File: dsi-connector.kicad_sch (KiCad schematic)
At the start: 13 parts, among them J1 Plug_Molex_SlimStack_2x20_556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

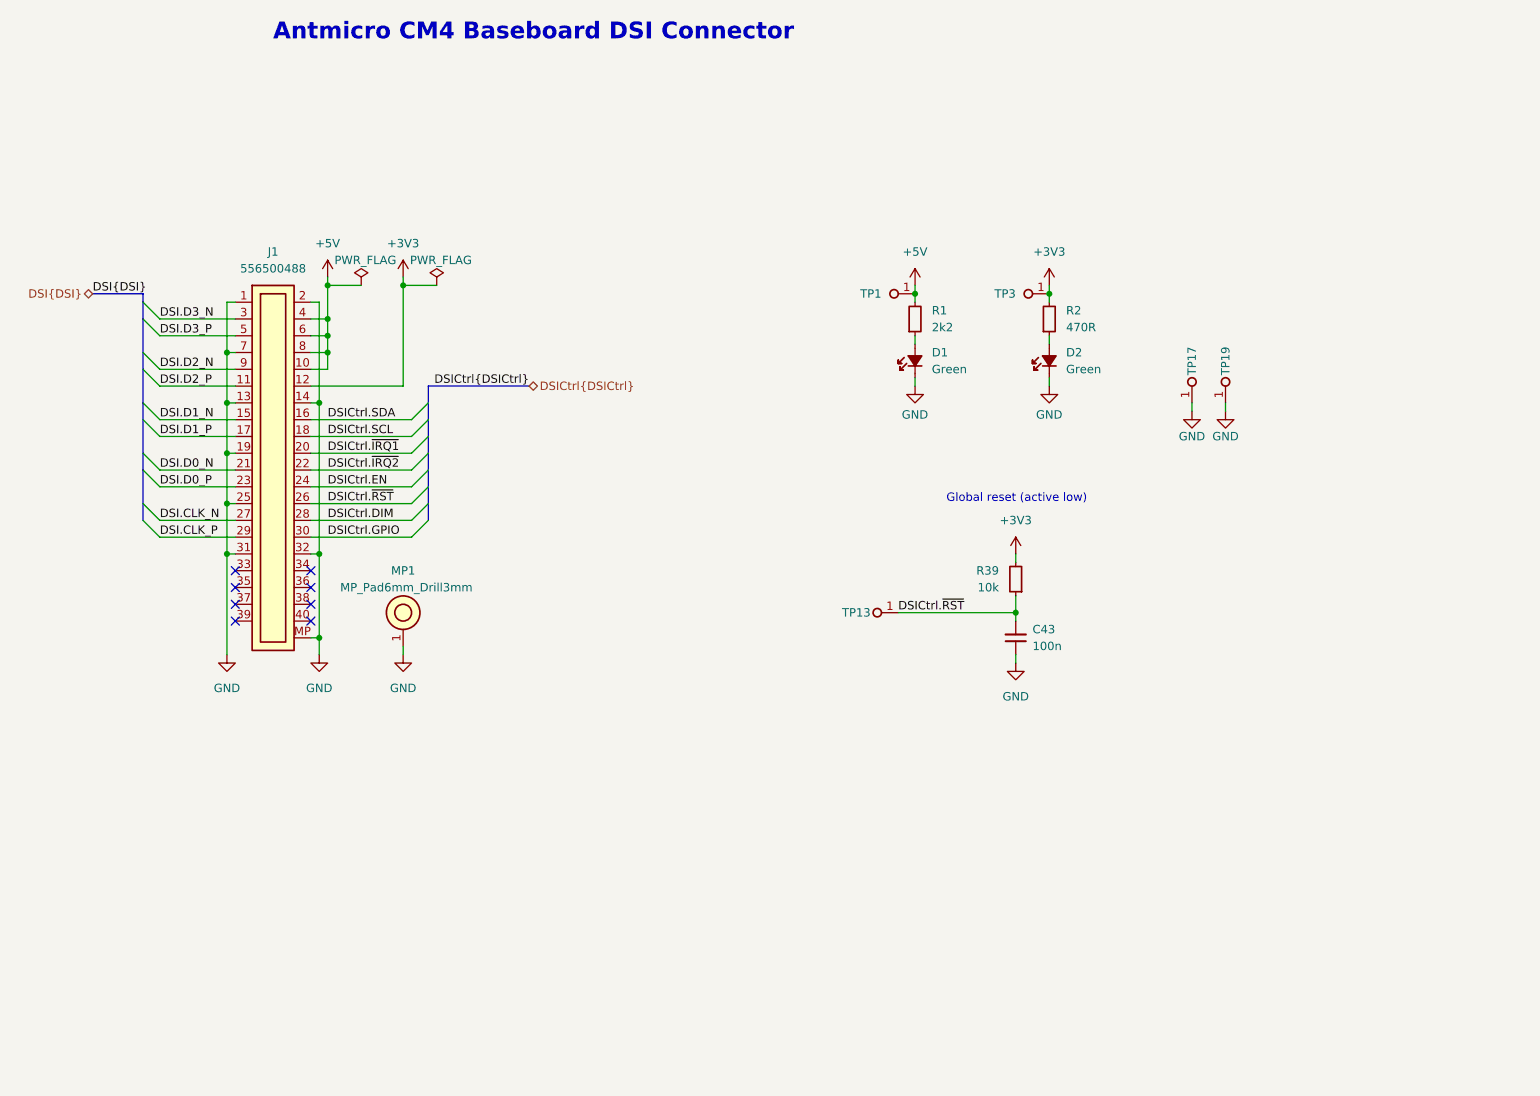
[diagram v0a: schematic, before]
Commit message: [#73840] Bump rev to 1.1.3, Standarize Sch
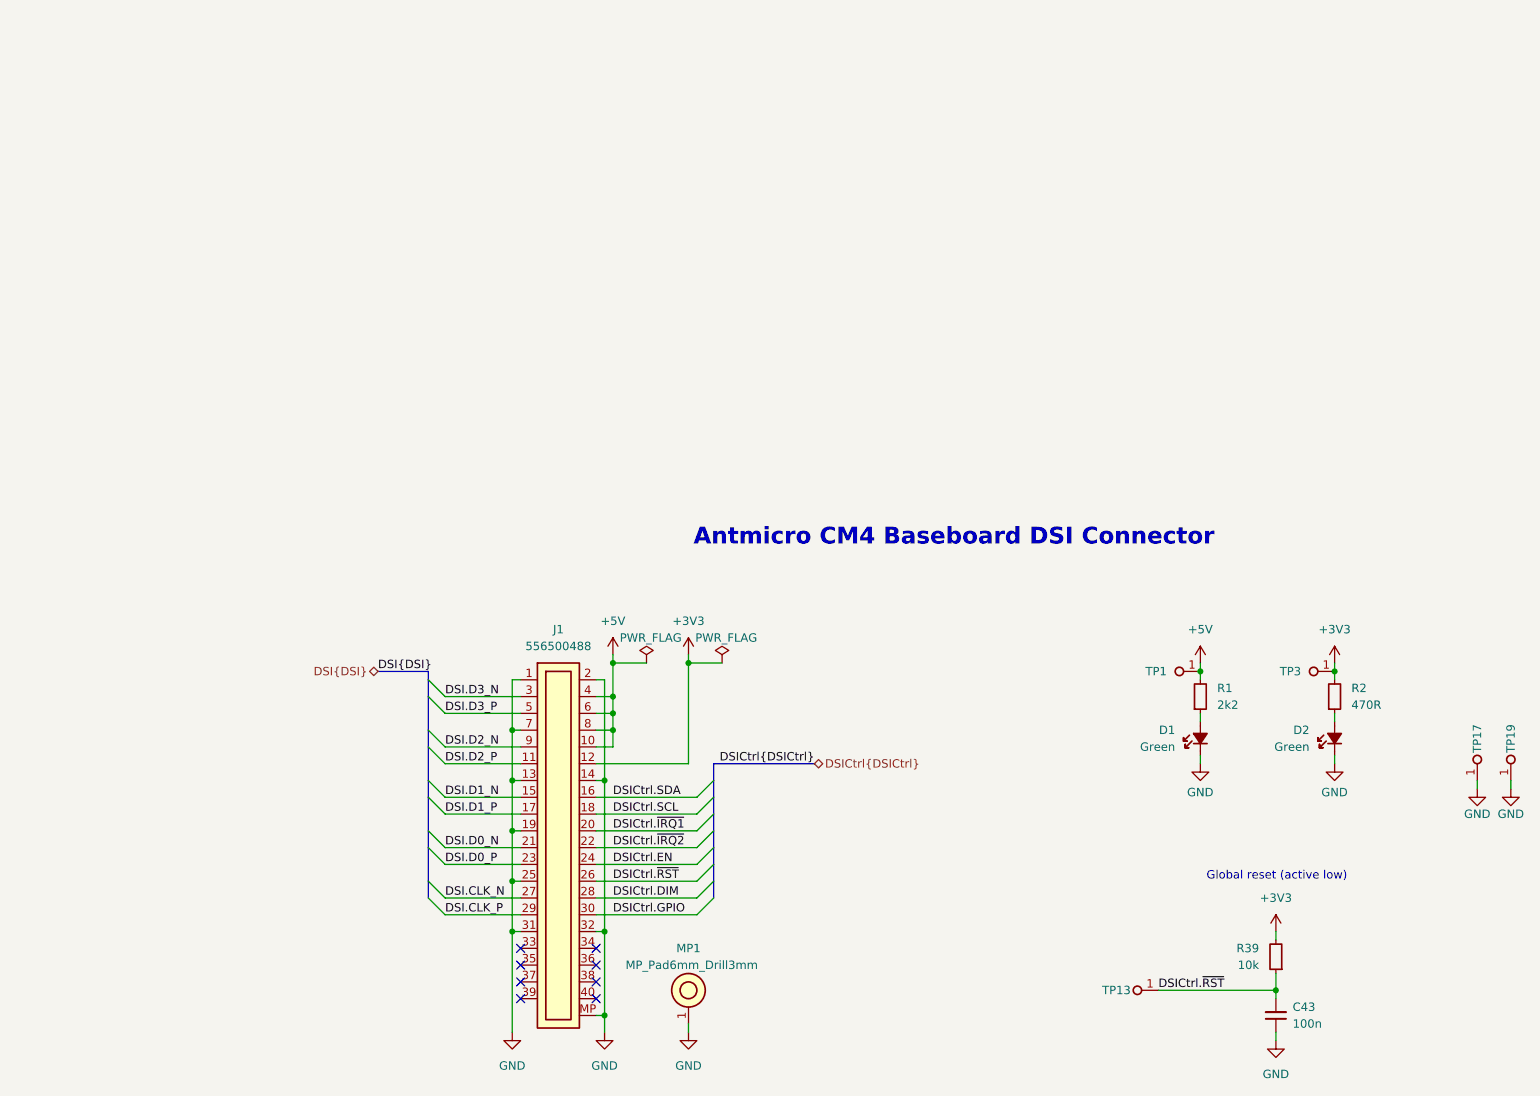
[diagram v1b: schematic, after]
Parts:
- C43, MP1, R1, R2, R39, TP1, TP3: Public False -> (none)
- D1, D2: footprint antmicro-footprints:LED_0603_1608Metric_G -> antmicro-footprints:LED_0603_1608Metric_G_Right_Angle; Public False -> (none)
- TP13, TP17, TP19: Public False -> (none); now left out of the parts list
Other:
- moved on the sheet: C43, D1, D2, J1, MP1, R1, R2, R39, TP1, TP13, TP17, TP19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

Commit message: [#73840] Change right angle LEDs to vertical (KP-1608ZGC)
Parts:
- removed D1, D2: LED_G_0603_598-8D80-107F, antmicro-footprints:LED_0603_1608Metric_G_Right_Angle, symbol antmicroLEDIndicationDiscrete:LED_G_0603_598-8D80-107F
- removed R1: R_2k2_0402, antmicro-footprints:R_0402_1005Metric, symbol antmicroResistors0402:R_2k2_0402
- removed R2: R_470R_0402, antmicro-footprints:R_0402_1005Metric, symbol antmicroResistors0402:R_470R_0402
- added D1, D2: LED_G_0603_KP-1608ZGC, antmicro-footprints:LED_0603_1608Metric_G, symbol antmicroLEDIndicationDiscrete:LED_G_0603_KP-1608ZGC
- added R1: R_470R_0402, antmicro-footprints:R_0402_1005Metric, symbol antmicroResistors0402:R_470R_0402
- added R3: R_330R_0402, antmicro-footprints:R_0402_1005Metric, symbol antmicroResistors0402:R_330R_0402
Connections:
- net +3V3: now also R3.2
- net +5V: now also R1.2
- net GND: now also D1.1 (C), D2.1 (C)
- new net: D2.2 (A), R3.1
- new net: D1.2 (A), R1.1

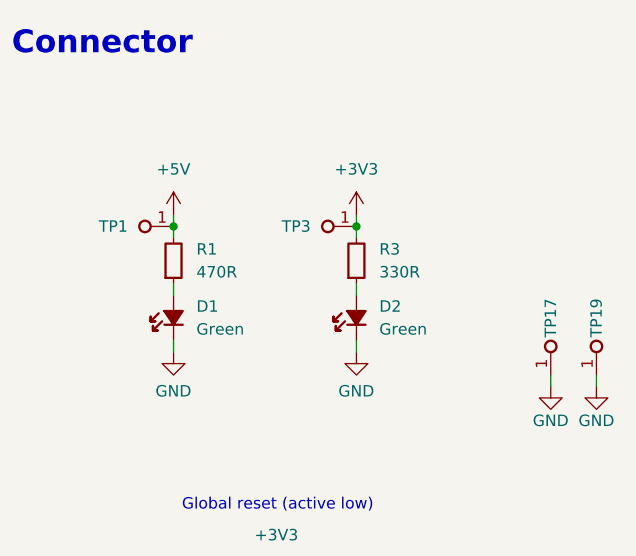
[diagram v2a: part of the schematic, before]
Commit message: [#73840] Update 3V3 LED resistors to 100R andd 10V5 LED resistors to 1k5
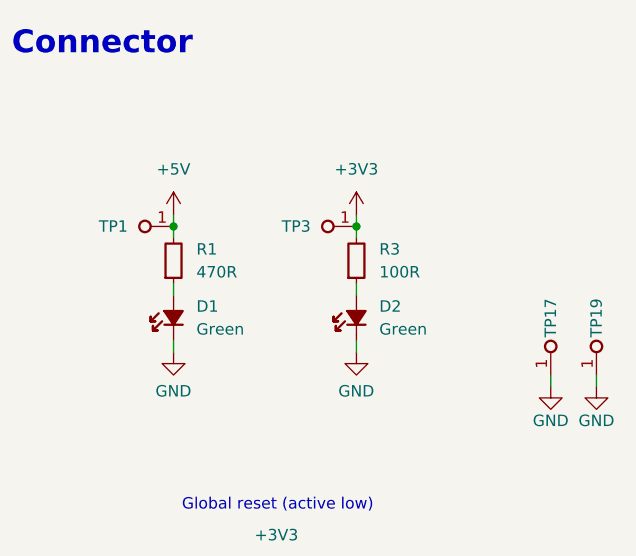
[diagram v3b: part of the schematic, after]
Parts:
- removed R3: R_330R_0402, antmicro-footprints:R_0402_1005Metric, symbol antmicroResistors0402:R_330R_0402
- added R3: R_100R_0402, antmicro-footprints:R_0402_1005Metric, symbol antmicroResistors0402:R_100R_0402
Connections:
- net +3V3: now also R3.2
- net at D2.2 (A): now also R3.1
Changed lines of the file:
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@@
+	)
+	(symbol
+		(lib_id "antmicroResistors0402:R_100R_0402")
+		(at 270.51 124.46 90)
+		(unit 1)
+		(exclude_from_sim no)
+		(in_bom yes)
+		(on_board yes)
+		(dnp no)
+		(fields_autoplaced yes)
+		(property "Reference" "R3"
+			(at 273.05 120.65 90)
+			(effects
+				(font
+					(size 1.27 1.27)
+					(thickness 0.15)
+				)
+				(justify right)
+			)
+		)
+		(property "Value" "R_100R_0402"
+			(at 283.21 104.14 0)
+			(effects
+				(font
+					(size 1.27 1.27)
+					(thickness 0.15)
+				)
+				(justify left bottom)
+				(hide yes)
+			)
+		)
+		(property "Footprint" "antmicro-footprints:R_0402_1005Metric"
+			(at 285.75 104.14 0)
+			(effects
+				(font
+					(size 1.27 1.27)
+					(thickness 0.15)
+				)
+				(justify left bottom)
+				(hide yes)
+			)
+		)
+		(property "Datasheet" "https://www.bourns.com/docs/product-datasheets/cr.pdf"
+			(at 288.29 104.14 0)
+			(effects
+				(font
+					(size 1.27 1.27)
+					(thickness 0.15)
+				)
+				(justify left bottom)
+				(hide yes)
+			)
+		)
+		(property "Description" "SMD Chip Resistor, 100 ohm, ± 1%, 62.5 mW, 0402 [1005 Metric], Thick Film, General Purpose"
+			(at 270.51 124.46 0)
+			(effects
+				(font
+					(size 1.27 1.27)
+				)
+				(hide yes)
+			)
+		)
+		(property "MPN" "CR0402-FX-1000GLF"
+			(at 290.83 104.14 0)
+			(effects
+				(font
+					(size 1.27 1.27)
+					(thickness 0.15)
+				)
+				(justify left bottom)
+				(hide yes)
+			)
+		)
+		(property "Manufacturer" "Bourns"
+			(at 293.37 104.14 0)
+			(effects
+				(font
+					(size 1.27 1.27)
+					(thickness 0.15)
+				)
+				(justify left bottom)
+				(hide yes)
+			)
+		)
+		(property "License" "Apache-2.0"
+			(at 295.91 104.14 0)
+			(effects
+				(font
+					(size 1.27 1.27)
+					(thickness 0.15)
+				)
+				(justify left bottom)
+				(hide yes)
+			)
+		)
+		(property "Author" "Antmicro"
+			(at 298.45 104.14 0)
+			(effects
+				(font
+					(size 1.27 1.27)
+					(thickness 0.15)
+				)
+				(justify left bottom)
+				(hide yes)
+			)
+		)
+		(property "Val" "100R"
+			(at 273.05 123.19 90)
+			(effects
+				(font
+					(size 1.27 1.27)
+					(thickness 0.15)
+				)
+				(justify right)
+			)
+		)
+		(property "Tolerance" "1%"
+			(at 280.67 104.14 0)
+			(effects
+				(font
+					(size 1.27 1.27)
+				)
+				(justify left bottom)
+				(hide yes)
+			)
+		)
+		(pin "2"
+		)
+		(pin "1"
+		)
+		(instances
+			(project ""
+				(path "/60b842dc-0853-4a25-99ac-5784ddf94d0d/22d16469-9258-4636-9009-0bef153eb515"
+					(reference "R3")
+					(unit 1)
+				)
+			)
+		)
 	)
 	(symbol
@@
 					(unit 1)
 				)
-			)
-		)
-	)
-	(symbol
-		(lib_id "antmicroResistors0402:R_330R_0402")
-		(at 270.51 124.46 90)
-		(unit 1)
-		(exclude_from_sim no)
-		(in_bom yes)
-		(on_board yes)
-		(dnp no)
-		(fields_autoplaced yes)
-		(property "Reference" "R3"
-			(at 273.05 120.65 90)
-			(effects
-				(font
-					(size 1.27 1.27)
-					(thickness 0.15)
-				)
-				(justify right)
-			)
-		)
-		(property "Value" "R_330R_0402"
-			(at 283.21 104.14 0)
-			(effects
-				(font
-					(size 1.27 1.27)
-					(thickness 0.15)
-				)
-				(justify left bottom)
-				(hide yes)
-			)
-		)
-		(property "Footprint" "antmicro-footprints:R_0402_1005Metric"
-			(at 285.75 104.14 0)
-			(effects
-				(font
-					(size 1.27 1.27)
-					(thickness 0.15)
-				)
-				(justify left bottom)
-				(hide yes)
-			)
-		)
-		(property "Datasheet" "https://www.bourns.com/docs/product-datasheets/cr.pdf"
-			(at 288.29 104.14 0)
-			(effects
-				(font
-					(size 1.27 1.27)
-					(thickness 0.15)
-				)
-				(justify left bottom)
-				(hide yes)
-			)
-		)
-		(property "Description" "SMD Chip Resistor, 330 ohm, ± 1%, 62.5 mW, 0402 [1005 Metric], Thick Film, General Purpose"
-			(at 270.51 124.46 0)
-			(effects
-				(font
-					(size 1.27 1.27)
-				)
-				(hide yes)
-			)
-		)
-		(property "MPN" "CR0402-FX-3300GLF"
-			(at 290.83 104.14 0)
-			(effects
-				(font
-					(size 1.27 1.27)
-					(thickness 0.15)
-				)
-				(justify left bottom)
-				(hide yes)
-			)
-		)
-		(property "Manufacturer" "Bourns"
-			(at 293.37 104.14 0)
-			(effects
-				(font
-					(size 1.27 1.27)
-					(thickness 0.15)
-				)
-				(justify left bottom)
-				(hide yes)
-			)
-		)
-		(property "License" "Apache-2.0"
-			(at 295.91 104.14 0)
-			(effects
-				(font
-					(size 1.27 1.27)
-					(thickness 0.15)
-				)
-				(justify left bottom)
-				(hide yes)
-			)
-		)
-		(property "Author" "Antmicro"
-			(at 298.45 104.14 0)
-			(effects
-				(font
-					(size 1.27 1.27)
-					(thickness 0.15)
-				)
-				(justify left bottom)
-				(hide yes)
-			)
-		)
-		(property "Val" "330R"
-			(at 273.05 123.19 90)
-			(effects
-				(font
-					(size 1.27 1.27)
-					(thickness 0.15)
-				)
-				(justify right)
-			)
-		)
-		(property "Tolerance" "1%"
-			(at 280.67 104.14 0)
-			(effects
-				(font
-					(size 1.27 1.27)
-				)
-				(justify left bottom)
-				(hide yes)
-			)
-		)
-		(pin "1"
-		)
-		(pin "2"
-		)
-		(instances
-			(project ""
-				(path "/60b842dc-0853-4a25-99ac-5784ddf94d0d/22d16469-9258-4636-9009-0bef153eb515"
-					(reference "R3")
-					(unit 1)
-				)
